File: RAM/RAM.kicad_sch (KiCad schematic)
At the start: 36 parts, among them J1 Conn_01x02_Pin, J2 Conn_01x02_Pin, J3 Conn_01x04_Pin, J4 Conn_01x06_Pin, J5 Conn_01x08_Socket, J6 Conn_01x03_Pin, J7 Conn_01x03_Pin, J8 Conn_01x01_Pin, J9 Conn_01x01_Pin, U2 CD74HCT258E, U3 SN74HCT245N, U4 CD74HCT258E, U6 CD74HCT258E

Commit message: Updated RAM pin headers to 2.54mm and correct assignment
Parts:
- removed J3: Conn_01x04_Pin, Connector_PinHeader_1.00mm:PinHeader_1x04_P1.00mm_Horizontal, symbol Connector:Conn_01x04_Pin
- removed J4: Conn_01x06_Pin, Connector_PinHeader_1.00mm:PinHeader_1x06_P1.00mm_Horizontal, symbol Connector:Conn_01x06_Pin
- removed J5: Conn_01x08_Socket, Connector_PinHeader_1.00mm:PinHeader_1x08_P1.00mm_Horizontal, symbol Connector:Conn_01x08_Socket
- added J5: Conn_01x05_Pin, Connector_PinHeader_2.54mm:PinHeader_1x05_P2.54mm_Vertical, symbol Connector:Conn_01x05_Pin
- added J8: Conn_01x03_Pin, Connector_PinHeader_2.54mm:PinHeader_1x03_P2.54mm_Vertical, symbol Connector:Conn_01x03_Pin
- added J9: Conn_01x10_Pin, Connector_PinHeader_2.54mm:PinHeader_1x10_P2.54mm_Vertical, symbol Connector:Conn_01x10_Pin
- J1: footprint Connector_PinHeader_1.00mm:PinHeader_1x02_P1.00mm_Vertical -> Connector_PinHeader_2.54mm:PinHeader_1x02_P2.54mm_Vertical
- J2: renamed from J8; footprint Connector_PinHeader_1.00mm:PinHeader_1x01_P1.00mm_Vertical -> Connector_PinHeader_2.54mm:PinHeader_1x01_P2.54mm_Vertical
- J3: renamed from J2; footprint Connector_PinHeader_1.00mm:PinHeader_1x02_P1.00mm_Vertical -> Connector_PinHeader_2.54mm:PinHeader_1x02_P2.54mm_Vertical
- J4: renamed from J9; footprint Connector_PinHeader_1.00mm:PinHeader_1x01_P1.00mm_Vertical -> Connector_PinHeader_2.54mm:PinHeader_1x01_P2.54mm_Vertical
- J6, J7: footprint Connector_PinHeader_1.00mm:PinHeader_1x03_P1.00mm_Vertical -> Connector_PinHeader_2.54mm:PinHeader_1x03_P2.54mm_Vertical
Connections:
- net +5V: now also J9.1 (Pin_1)
- net A0: now also J5.4 (Pin_4)
- net A1: now also J5.3 (Pin_3)
- net A2: now also J5.2 (Pin_2)
- net A3: now also J5.1 (Pin_1)
- net Bus 0: now also J9.3 (Pin_3)
- net Bus 1: now also J9.4 (Pin_4)
- net Bus 2: now also J9.5 (Pin_5)
- net Bus 3: now also J9.6 (Pin_6)
- net Bus 4: now also J9.7 (Pin_7)
- net Bus 5: now also J9.8 (Pin_8)
- net Bus 6: now also J9.9 (Pin_9)
- net Bus 7: now also J9.10 (Pin_10)
- net CLK: now also J8.2 (Pin_2)
- net GND: now also J9.2 (Pin_2)
- net Program: now also J5.5 (Pin_5)
- net Read in: now also J8.3 (Pin_3)
- net ~Read out: now also J8.1 (Pin_1)

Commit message: Updated RAM LED footprints
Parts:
- D1, D2, D3, D4, D5, D6, D7, D8: footprint LED_THT:LED_D2.0mm_W4.8mm_H2.5mm_FlatTop -> LED_THT:LED_D5.0mm
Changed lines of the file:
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@@
 			)
 		)
-		(property "Footprint" "LED_THT:LED_D2.0mm_W4.8mm_H2.5mm_FlatTop"
+		(property "Footprint" "LED_THT:LED_D5.0mm"
 			(at 173.99 133.35 0)
 			(effects
@@
 			)
 		)
-		(property "Footprint" "LED_THT:LED_D2.0mm_W4.8mm_H2.5mm_FlatTop"
+		(property "Footprint" "LED_THT:LED_D5.0mm"
 			(at 151.13 133.35 0)
 			(effects
@@
 			)
 		)
-		(property "Footprint" "LED_THT:LED_D2.0mm_W4.8mm_H2.5mm_FlatTop"
+		(property "Footprint" "LED_THT:LED_D5.0mm"
 			(at 128.27 133.35 0)
 			(effects
@@
 			)
 		)
-		(property "Footprint" "LED_THT:LED_D2.0mm_W4.8mm_H2.5mm_FlatTop"
+		(property "Footprint" "LED_THT:LED_D5.0mm"
 			(at 181.61 133.35 0)
 			(effects
@@
 			)
 		)
-		(property "Footprint" "LED_THT:LED_D2.0mm_W4.8mm_H2.5mm_FlatTop"
+		(property "Footprint" "LED_THT:LED_D5.0mm"
 			(at 135.89 133.35 0)
 			(effects
@@
 			)
 		)
-		(property "Footprint" "LED_THT:LED_D2.0mm_W4.8mm_H2.5mm_FlatTop"
+		(property "Footprint" "LED_THT:LED_D5.0mm"
 			(at 143.51 133.35 0)
 			(effects
@@
 			)
 		)
-		(property "Footprint" "LED_THT:LED_D2.0mm_W4.8mm_H2.5mm_FlatTop"
+		(property "Footprint" "LED_THT:LED_D5.0mm"
 			(at 166.37 133.35 0)
 			(effects
@@
 			)
 		)
-		(property "Footprint" "LED_THT:LED_D2.0mm_W4.8mm_H2.5mm_FlatTop"
+		(property "Footprint" "LED_THT:LED_D5.0mm"
 			(at 158.75 133.35 0)
 			(effects

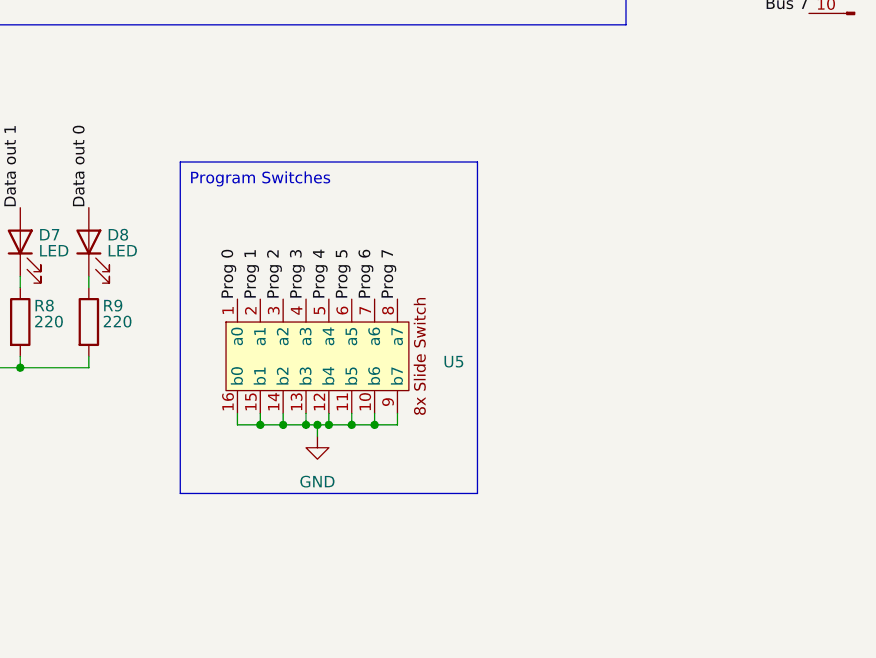
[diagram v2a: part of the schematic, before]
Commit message: Added pullup resistors to the programming switches
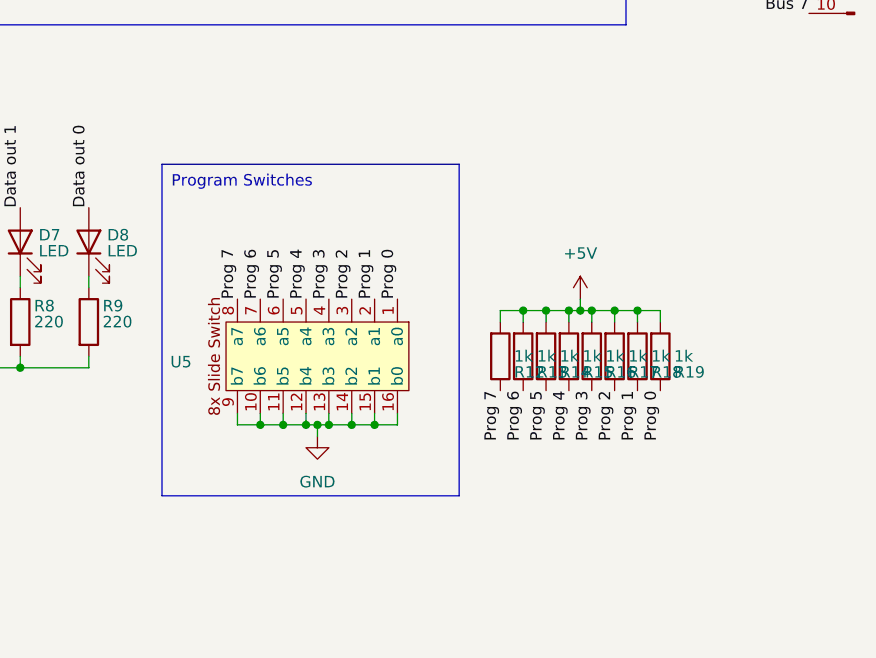
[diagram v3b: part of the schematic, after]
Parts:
- added R12, R13, R14, R15, R16, R17, R18, R19: 1k, _DownloadFootprints:CF_series_Resistors_THT, symbol Device:R
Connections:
- net +5V: now also R12.2, R13.2, R14.2, R15.2, R16.2, R17.2, R18.2, R19.2
- net Prog 0: now also R19.1
- net Prog 1: now also R18.1
- net Prog 2: now also R17.1
- net Prog 3: now also R16.1
- net Prog 4: now also R15.1
- net Prog 5: now also R14.1
- net Prog 6: now also R13.1
- net Prog 7: now also R12.1
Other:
- moved on the sheet: U5

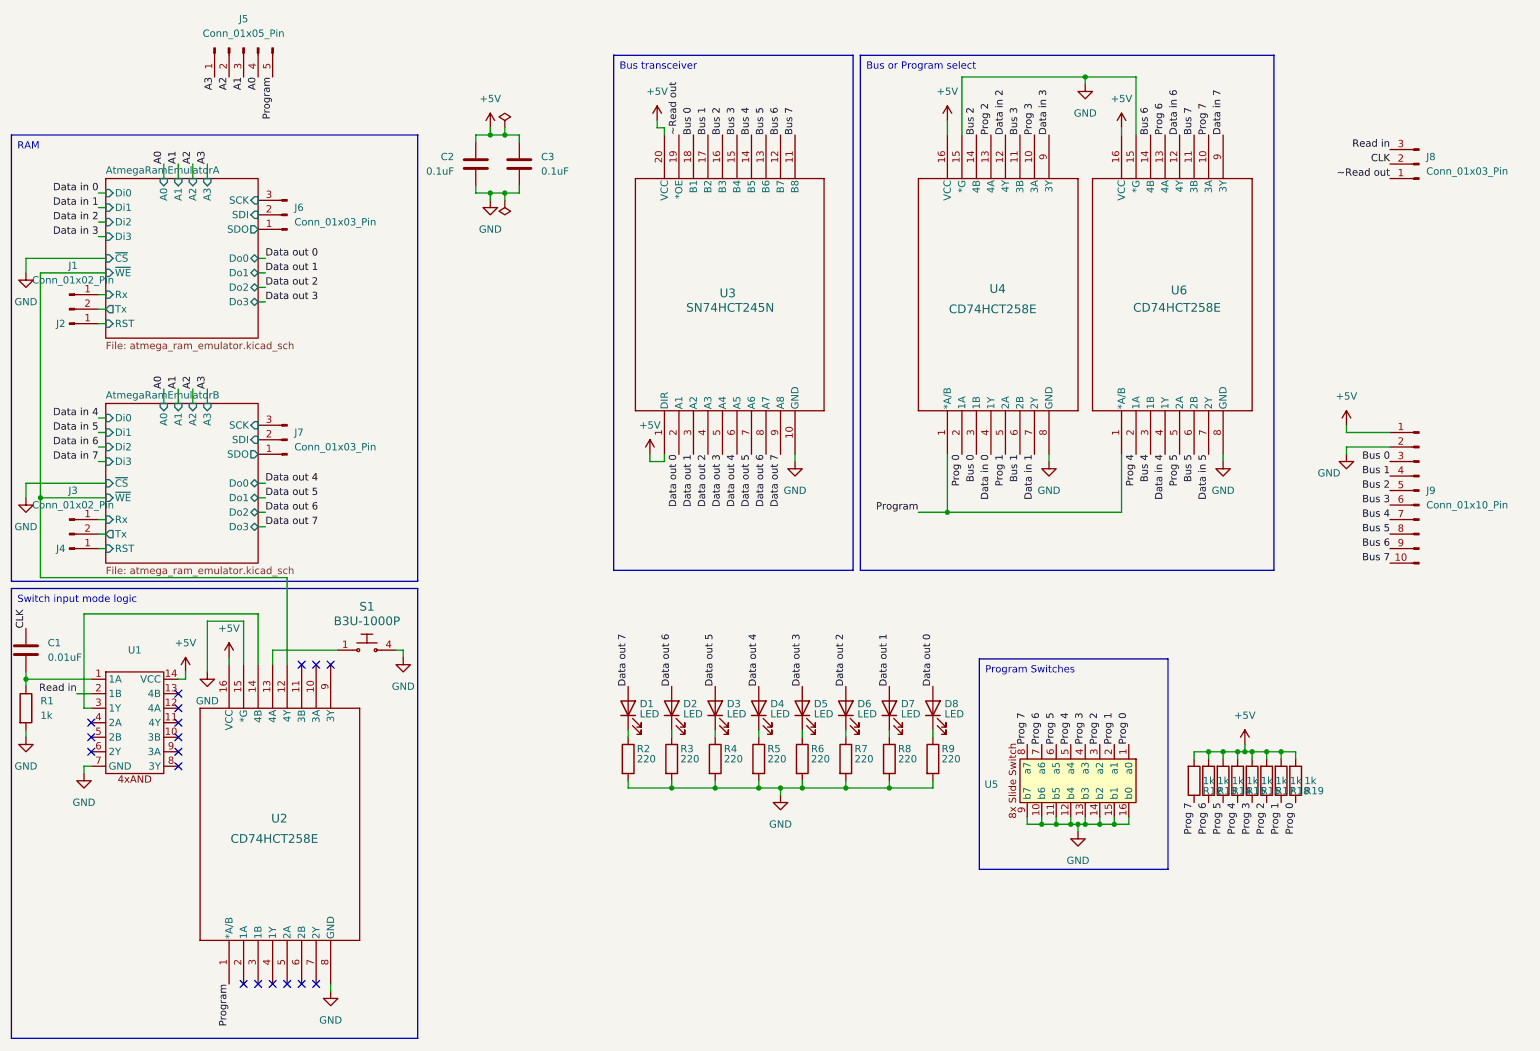
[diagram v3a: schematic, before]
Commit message: Fixed incorrect MUX inputs on RAM
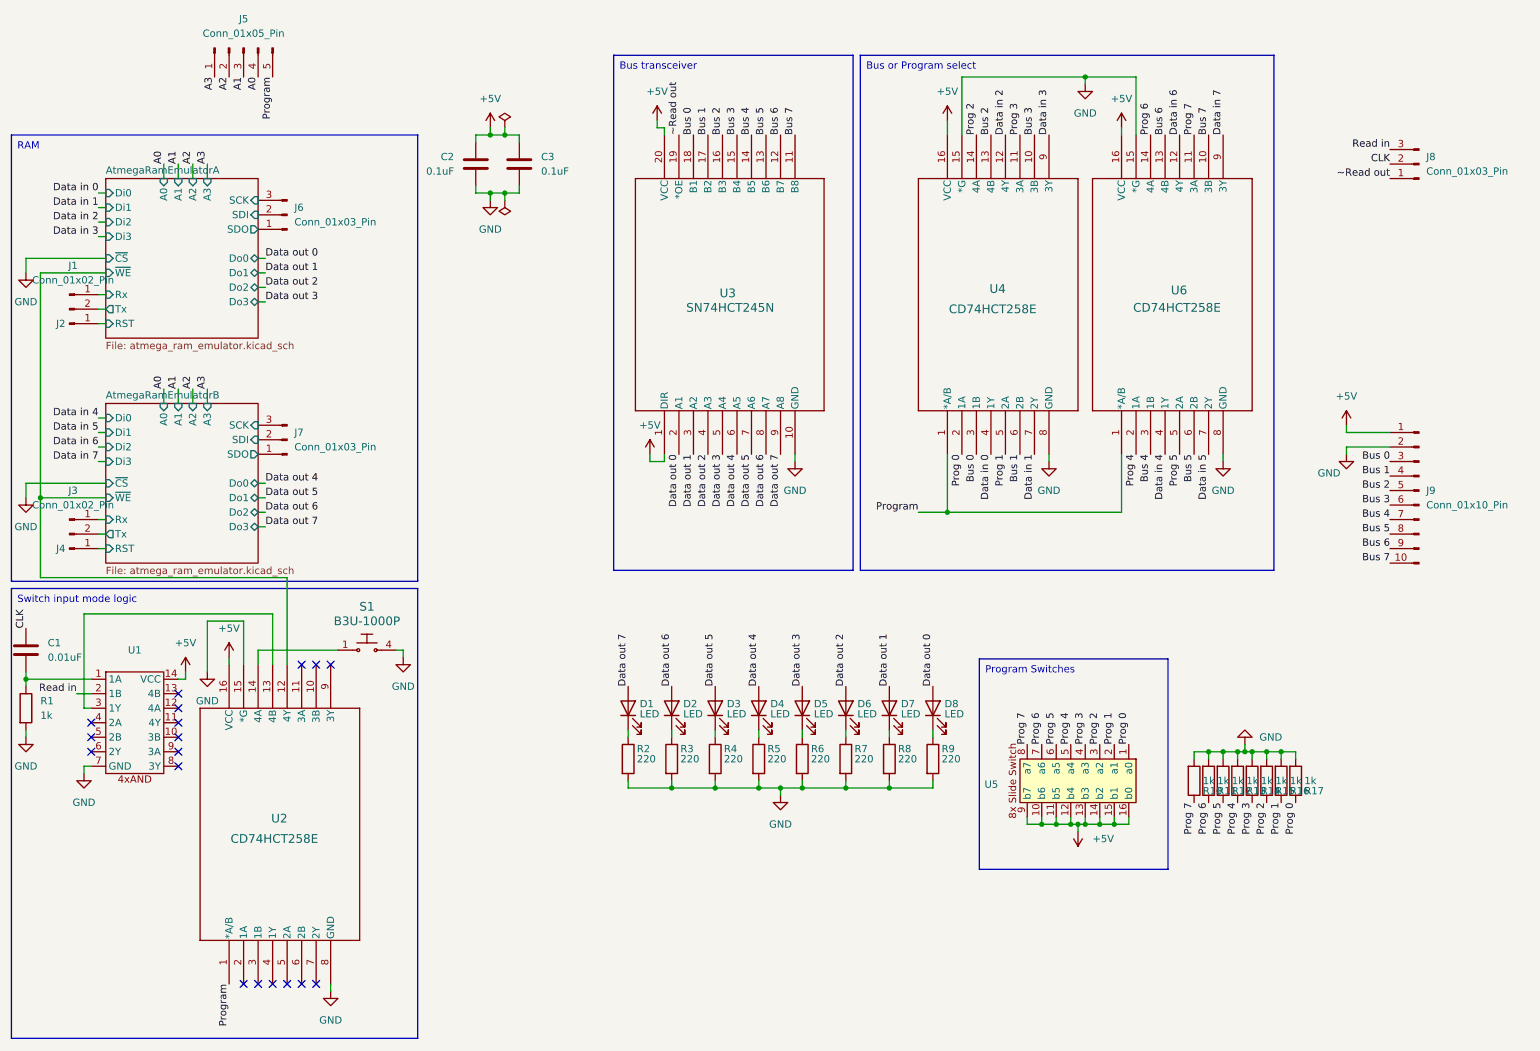
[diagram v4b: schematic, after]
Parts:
- renumbered R12 to R10, R13 to R11, R14 to R12, R15 to R13, R16 to R14, R17 to R15, R18 to R16, R19 to R17
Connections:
- net +5V: now also U5.10 (b6), U5.11 (b5), U5.12 (b4), U5.13 (b3), U5.14 (b2), U5.15 (b1), U5.16 (b0), U5.9 (b7); no longer R10.2, R11.2, R12.2, R13.2, R14.2, R15.2, R16.2, R17.2
- net Bus 2: now also U4.13 (4B); no longer U4.14 (4B)
- net Bus 3: now also U4.10 (3B); no longer U4.11 (3B)
- net Bus 6: now also U6.13 (4B); no longer U6.14 (4B)
- net Bus 7: now also U6.10 (3B); no longer U6.11 (3B)
- net GND: now also R10.2, R11.2, R12.2, R13.2, R14.2, R15.2, R16.2, R17.2; no longer U5.10 (b6), U5.11 (b5), U5.12 (b4), U5.13 (b3), U5.14 (b2), U5.15 (b1), U5.16 (b0), U5.9 (b7)
- net Prog 2: now also U4.14 (4A); no longer U4.13 (4A)
- net Prog 3: now also U4.11 (3A); no longer U4.10 (3A)
- net Prog 6: now also U6.14 (4A); no longer U6.13 (4A)
- net Prog 7: now also U6.11 (3A); no longer U6.10 (3A)
- net at U2.13 (4B): now also U1.3 (1Y); no longer S1.1
- net at U2.14 (4A): now also S1.1; no longer U1.3 (1Y)
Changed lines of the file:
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@@
 	(wire
 		(pts
+			(xy 63.5 123.19) (xy 63.5 125.73)
+		)
+		(stroke
+			(width 0)
+			(type default)
+		)
+	)
+	(wire
+		(pts
 			(xy 31.75 130.81) (xy 34.29 130.81)
 		)
@@
 	(wire
 		(pts
-			(xy 77.47 123.19) (xy 66.04 123.19)
-		)
-		(stroke
-			(width 0)
-			(type default)
-		)
-	)
-	(wire
-		(pts
 			(xy 213.36 152.4) (xy 213.36 153.67)
 		)
@@
 	(wire
 		(pts
+			(xy 63.5 123.19) (xy 77.47 123.19)
+		)
+		(stroke
+			(width 0)
+			(type default)
+		)
+	)
+	(wire
+		(pts
 			(xy 254 85.09) (xy 254 83.82)
 		)
@@
 	(wire
 		(pts
-			(xy 66.04 123.19) (xy 66.04 125.73)
-		)
-		(stroke
-			(width 0)
-			(type default)
-		)
-	)
-	(wire
-		(pts
 			(xy 227.33 142.24) (xy 227.33 140.97)
 		)
@@
 	(wire
 		(pts
-			(xy 63.5 116.84) (xy 63.5 125.73)
-		)
-		(stroke
-			(width 0)
-			(type default)
-		)
-	)
-	(wire
-		(pts
 			(xy 200.66 152.4) (xy 200.66 153.67)
 		)
@@
 	(wire
 		(pts
-			(xy 33.02 116.84) (xy 63.5 116.84)
+			(xy 33.02 116.84) (xy 66.04 116.84)
+		)
+		(stroke
+			(width 0)
+			(type default)
+		)
+	)
+	(wire
+		(pts
+			(xy 66.04 116.84) (xy 66.04 125.73)
 		)
 		(stroke
@@
 	)
 	(label "Prog 6"
-		(at 222.25 33.02 90)
+		(at 219.71 33.02 90)
 		(fields_autoplaced yes)
 		(effects
@@
 	)
 	(label "Prog 7"
-		(at 229.87 33.02 90)
+		(at 227.33 33.02 90)
 		(fields_autoplaced yes)
 		(effects
@@
 	)
 	(label "Bus 3"
-		(at 196.85 33.02 90)
+		(at 199.39 33.02 90)
 		(fields_autoplaced yes)
 		(effects
@@
 	)
 	(label "Bus 7"
-		(at 227.33 33.02 90)
+		(at 229.87 33.02 90)
 		(fields_autoplaced yes)
 		(effects
@@
 	)
 	(label "Bus 2"
-		(at 189.23 33.02 90)
+		(at 191.77 33.02 90)
 		(fields_autoplaced yes)
 		(effects
@@
 	)
 	(label "Bus 6"
-		(at 219.71 33.02 90)
+		(at 222.25 33.02 90)
 		(fields_autoplaced yes)
 		(effects
@@
 	)
 	(label "Prog 2"
-		(at 191.77 33.02 90)
+		(at 189.23 33.02 90)
 		(fields_autoplaced yes)
 		(effects
@@
 	)
 	(label "Prog 3"
-		(at 199.39 33.02 90)
+		(at 196.85 33.02 90)
 		(fields_autoplaced yes)
 		(effects
@@
 		(on_board yes)
 		(dnp no)
-		(property "Reference" "R15"
+		(property "Reference" "R13"
 			(at 236.474 147.828 0)
 			(effects
@@
 			(project "RAM"
 				(path "/5d332551-33f6-4491-a826-882274bc7f5d"
-					(reference "R15")
+					(reference "R13")
 					(unit 1)
 				)
@@
 		(on_board yes)
 		(dnp no)
-		(property "Reference" "#PWR023"
+		(property "Reference" "#PWR024"
 			(at 254 95.25 0)
 			(effects
@@
 			(project "RAM"
 				(path "/5d332551-33f6-4491-a826-882274bc7f5d"
-					(reference "#PWR023")
+					(reference "#PWR024")
 					(unit 1)
 				)
@@
 	(symbol
 		(lib_id "power:+5V")
-		(at 236.22 139.7 0)
+		(at 207.01 154.94 180)
 		(unit 1)
 		(exclude_from_sim no)
@@
 		(dnp no)
 		(fields_autoplaced yes)
-		(property "Reference" "#PWR032"
-			(at 236.22 143.51 0)
+		(property "Reference" "#PWR022"
+			(at 207.01 151.13 0)
 			(effects
 				(font
@@
 		)
 		(property "Value" "+5V"
-			(at 236.22 134.62 0)
+			(at 209.55 156.2099 0)
 			(effects
 				(font
 					(size 1.27 1.27)
 				)
+				(justify right)
 			)
 		)
 		(property "Footprint" ""
-			(at 236.22 139.7 0)
+			(at 207.01 154.94 0)
 			(effects
 				(font
@@
 		)
 		(property "Datasheet" ""
-			(at 236.22 139.7 0)
+			(at 207.01 154.94 0)
 			(effects
 				(font
@@
 		)
 		(property "Description" "Power symbol creates a global label with name \"+5V\""
-			(at 236.22 139.7 0)
+			(at 207.01 154.94 0)
 			(effects
 				(font
@@
 			(project ""
 				(path "/5d332551-33f6-4491-a826-882274bc7f5d"
-					(reference "#PWR032")
+					(reference "#PWR022")
 					(unit 1)
 				)
@@
 		(dnp no)
 		(fields_autoplaced yes)
-		(property "Reference" "#PWR022"
+		(property "Reference" "#PWR023"
 			(at 254 87.63 0)
 			(effects
@@
 			(project "RAM"
 				(path "/5d332551-33f6-4491-a826-882274bc7f5d"
-					(reference "#PWR022")
+					(reference "#PWR023")
 					(unit 1)
 				)
@@
 		(on_board yes)
 		(dnp no)
-		(property "Reference" "R18"
+		(property "Reference" "R16"
 			(at 244.094 147.828 0)
 			(effects
@@
 			(project "RAM"
 				(path "/5d332551-33f6-4491-a826-882274bc7f5d"
-					(reference "R18")
+					(reference "R16")
 					(unit 1)
 				)
@@
 		(on_board yes)
 		(dnp no)
-		(property "Reference" "R13"
+		(property "Reference" "R11"
 			(at 231.394 147.828 0)
 			(effects
@@
 			(project "RAM"
 				(path "/5d332551-33f6-4491-a826-882274bc7f5d"
-					(reference "R13")
+					(reference "R11")
 					(unit 1)
 				)
@@
 		(on_board yes)
 		(dnp no)
-		(property "Reference" "R17"
+		(property "Reference" "R15"
 			(at 241.554 147.828 0)
 			(effects
@@
 			(project "RAM"
 				(path "/5d332551-33f6-4491-a826-882274bc7f5d"
-					(reference "R17")
+					(reference "R15")
 					(unit 1)
 				)
@@
 		(on_board yes)
 		(dnp no)
-		(property "Reference" "R12"
+		(property "Reference" "R10"
 			(at 228.854 147.828 0)
 			(effects
@@
 			(project "RAM"
 				(path "/5d332551-33f6-4491-a826-882274bc7f5d"
-					(reference "R12")
+					(reference "R10")
 					(unit 1)
 				)
@@
 		(on_board yes)
 		(dnp no)
-		(property "Reference" "R16"
+		(property "Reference" "R14"
 			(at 239.014 147.828 0)
 			(effects
@@
 			(project "RAM"
 				(path "/5d332551-33f6-4491-a826-882274bc7f5d"
-					(reference "R16")
+					(reference "R14")
 					(unit 1)
 				)
@@
 		(on_board yes)
 		(dnp no)
-		(property "Reference" "R14"
+		(property "Reference" "R12"
 			(at 233.934 147.828 0)
 			(effects
@@
 			(project "RAM"
 				(path "/5d332551-33f6-4491-a826-882274bc7f5d"
-					(reference "R14")
+					(reference "R12")
 					(unit 1)
 				)
@@
 		(on_board yes)
 		(dnp no)
-		(property "Reference" "R19"
+		(property "Reference" "R17"
 			(at 246.634 147.828 0)
 			(effects
@@
 			(project "RAM"
 				(path "/5d332551-33f6-4491-a826-882274bc7f5d"
-					(reference "R19")
+					(reference "R17")
 					(unit 1)
 				)
@@
 	(symbol
 		(lib_id "power:GND")
-		(at 207.01 154.94 0)
+		(at 236.22 139.7 180)
 		(unit 1)
 		(exclude_from_sim no)
@@
 		(fields_autoplaced yes)
 		(property "Reference" "#PWR018"
-			(at 207.01 161.29 0)
+			(at 236.22 133.35 0)
 			(effects
 				(font
@@
 		)
 		(property "Value" "GND"
-			(at 207.01 160.02 0)
+			(at 238.76 138.4299 0)
 			(effects
 				(font
 					(size 1.27 1.27)
 				)
+				(justify right)
 			)
 		)
 		(property "Footprint" ""
-			(at 207.01 154.94 0)
+			(at 236.22 139.7 0)
 			(effects
 				(font
@@
 		)
 		(property "Datasheet" ""
-			(at 207.01 154.94 0)
+			(at 236.22 139.7 0)
 			(effects
 				(font
@@
 		)
 		(property "Description" "Power symbol creates a global label with name \"GND\" , ground"
-			(at 207.01 154.94 0)
+			(at 236.22 139.7 0)
 			(effects
 				(font

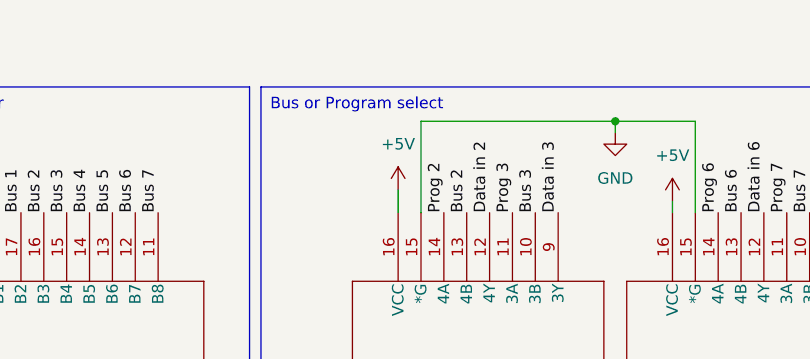
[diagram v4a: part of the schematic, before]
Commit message: Made atmega RAM emulators invert the data, because the selector is inverting it on the way in. Also fixed bug using WE pin inverted.
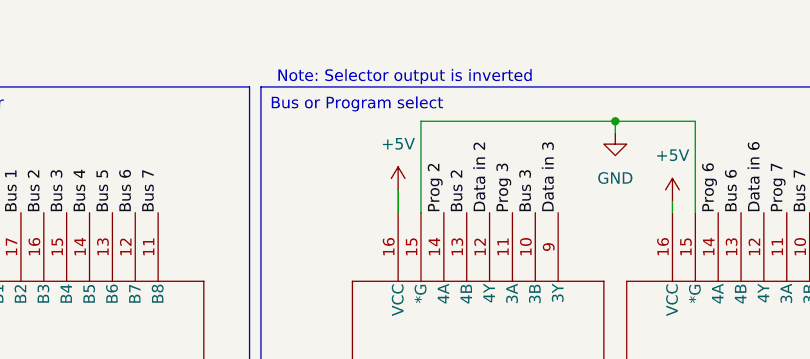
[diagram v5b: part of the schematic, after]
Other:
- note added: "Note: Selector output is inverted"
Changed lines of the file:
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@@
+		)
+	)
+	(text "Note: Selector output is inverted"
+		(exclude_from_sim no)
+		(at 184.912 18.034 0)
+		(effects
+			(font
+				(size 1.27 1.27)
+				(color 255 0 0 1)
+			)
 		)
 	)
